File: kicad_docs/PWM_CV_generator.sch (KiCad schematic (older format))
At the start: 6 parts, among them U5 TL072

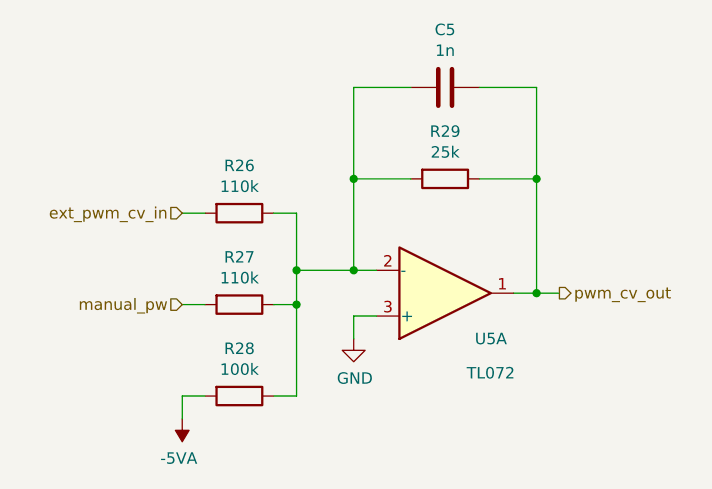
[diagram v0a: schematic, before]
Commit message: reduce amt of weird resistor vals
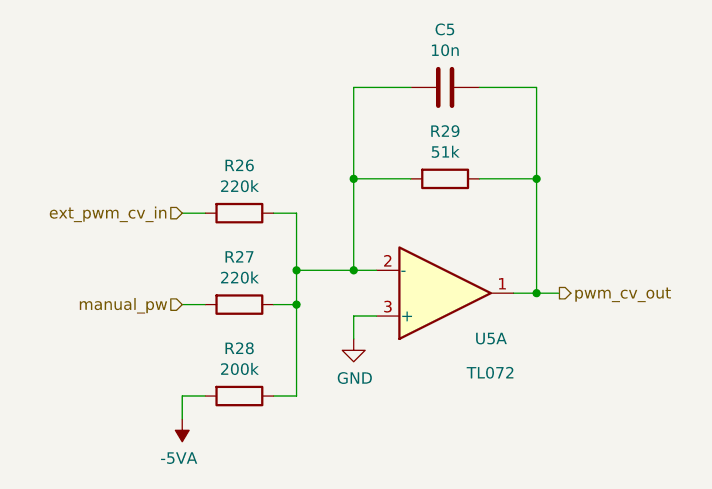
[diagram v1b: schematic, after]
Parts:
- C5: value 1n -> 10n
- R26, R27: value 110k -> 220k
- R28: value 100k -> 200k
- R29: value 25k -> 51k
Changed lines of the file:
@@
 $Descr A4 11693 8268
 encoding utf-8
-Sheet 4 6
+Sheet 3 6
 Title "SSI2130 VCO"
 Date "2021-12-23"
@@
 AR Path="/6233ADA3/623C0AFC" Ref="R29"  Part="1"
 F 0 "R29" V 5993 3450 50  0000 C CNN
-F 1 "25k" V 6084 3450 50  0000 C CNN
+F 1 "51k" V 6084 3450 50  0000 C CNN
 F 2 "Resistor_SMD:R_0805_2012Metric" V 6130 3450 50  0001 C CNN
 F 3 "~" H 6200 3450 50  0001 C CNN
@@
 AR Path="/6233ADA3/623C0B02" Ref="R26"  Part="1"
 F 0 "R26" V 5093 3600 50  0000 C CNN
-F 1 "110k" V 5184 3600 50  0000 C CNN
+F 1 "220k" V 5184 3600 50  0000 C CNN
 F 2 "Resistor_SMD:R_0805_2012Metric" V 5230 3600 50  0001 C CNN
 F 3 "~" H 5300 3600 50  0001 C CNN
@@
 AR Path="/6233ADA3/623C0B10" Ref="R28"  Part="1"
 F 0 "R28" V 5093 4400 50  0000 C CNN
-F 1 "100k" V 5184 4400 50  0000 C CNN
+F 1 "200k" V 5184 4400 50  0000 C CNN
 F 2 "Resistor_SMD:R_0805_2012Metric" V 5230 4400 50  0001 C CNN
 F 3 "~" H 5300 4400 50  0001 C CNN
@@
 AR Path="/6233ADA3/623CB748" Ref="R27"  Part="1"
 F 0 "R27" V 5093 4000 50  0000 C CNN
-F 1 "110k" V 5184 4000 50  0000 C CNN
+F 1 "220k" V 5184 4000 50  0000 C CNN
 F 2 "Resistor_SMD:R_0805_2012Metric" V 5230 4000 50  0001 C CNN
 F 3 "~" H 5300 4000 50  0001 C CNN
@@
 P 6200 3050
 F 0 "C5" V 5948 3050 50  0000 C CNN
-F 1 "1n" V 6039 3050 50  0000 C CNN
+F 1 "10n" V 6039 3050 50  0000 C CNN
 F 2 "Capacitor_SMD:C_0805_2012Metric" H 6238 2900 50  0001 C CNN
 F 3 "~" H 6200 3050 50  0001 C CNN
@@
 Connection ~ 5800 3450
 $Comp
-L power:-5VA #PWR?
+L power:-5VA #PWR0101
 U 1 1 61D2D3E1
 P 5050 4500
-F 0 "#PWR?" H 5050 4600 50  0001 C CNN
+F 0 "#PWR0101" H 5050 4600 50  0001 C CNN
 F 1 "-5VA" H 5065 4673 50  0000 C CNN
 F 2 "" H 5050 4500 50  0001 C CNN
